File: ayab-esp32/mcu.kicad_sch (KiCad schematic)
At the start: 29 parts, among them J201 SPARE1, J202 SPARE0, Q201 AO3400A, SW201 USER, SW202 RESET, SW203 BOOTSEL, U201 ESP32-S3-MINI-1

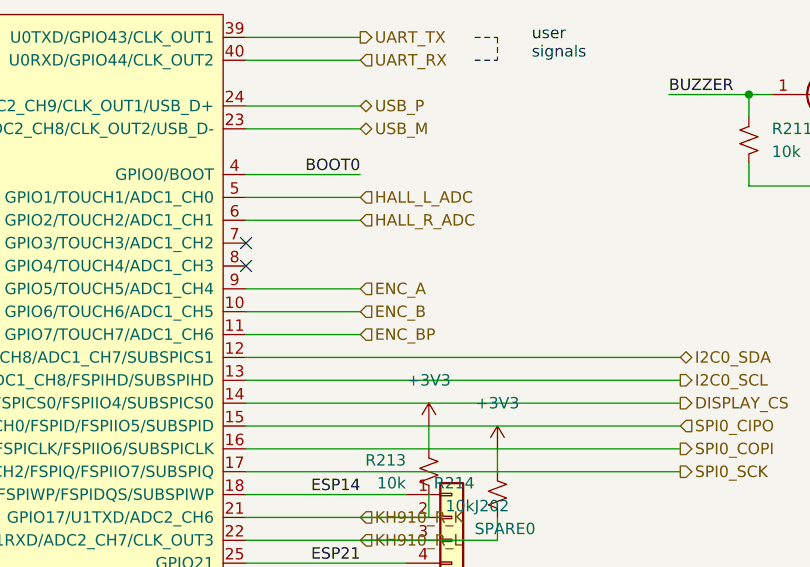
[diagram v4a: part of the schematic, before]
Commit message: Add machine power sensing on GPIO4
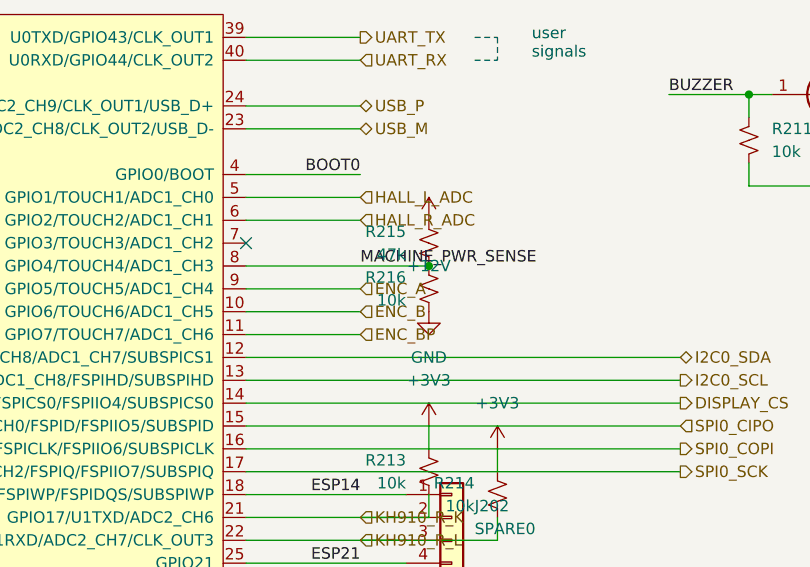
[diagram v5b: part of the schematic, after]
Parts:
- added R215: 47k, Resistor_SMD:R_0603_1608Metric, symbol ayab-lib:R_Small_US
- added R216: 10k, Resistor_SMD:R_0603_1608Metric, symbol ayab-lib:R_Small_US
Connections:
- net GND: now also R216.2
- net MACHINE_PWR_SENSE: now reaches U201.8 (GPIO4/TOUCH4/ADC1_CH3)
- net MACHINE_PWR_SENSE: now also R215.2, R216.1
- new net +12V: R215.1
- no-connect marks 8 -> 7
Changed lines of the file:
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@@
   (junction (at 41.91 99.06) (diameter 0) (color 0 0 0 0)
   )
-  (no_connect (at 185.42 82.55))
   (no_connect (at 185.42 80.01))
   (no_connect (at 93.98 128.27))
@@
   (no_connect (at 259.08 44.45))
   (no_connect (at 93.98 115.57))
+  (wire (pts (xy 185.42 82.55) (xy 205.74 82.55))
+    (stroke (width 0) (type default))
+  )
+  (junction (at 205.74 82.55) (diameter 0) (color 0 0 0 0)
+  )
+  (label "MACHINE_PWR_SENSE" (at 198.12 82.55 0) (fields_autoplaced)
+    (effects (font (size 1.27 1.27)) (justify left bottom))
+  )
   (wire (pts (xy 87.63 45.72) (xy 87.63 57.15))
     (stroke (width 0) (type default))
@@
         )
       )
+    )
+  )
+(symbol (lib_id "ayab-lib:R_Small_US") (at 205.74 80.01 0) (unit 1)
+    (in_bom yes) (on_board yes) (dnp no)
+    (property "Reference" "R215" (at 203.2 78.74 0)
+      (effects (font (size 1.27 1.27)) (justify right))
+    )
+    (property "Value" "47k" (at 203.2 81.28 0)
+      (effects (font (size 1.27 1.27)) (justify right))
+    )
+    (property "Footprint" "Resistor_SMD:R_0603_1608Metric" (at 205.74 80.01 0)
+      (effects (font (size 1.27 1.27)) hide)
+    )
+    (property "Datasheet" "~" (at 205.74 80.01 0)
+      (effects (font (size 1.27 1.27)) hide)
+    )
+    (property "LCSC ID" "C25819" (at 205.74 80.01 0)
+      (effects (font (size 1.27 1.27)) hide)
+    )
+    (property "Voltage rating" "" (at 205.74 80.01 0)
+      (effects (font (size 1.27 1.27)) hide)
+    )
+    (property "Package" "0603" (at 205.74 80.01 0)
+      (effects (font (size 1.27 1.27)) hide)
+    )
+    (property "OEM PN" "0603WAF4702T5E" (at 205.74 80.01 0)
+      (effects (font (size 1.27 1.27)) hide)
+    )
+    (property "OEM" "UNI-ROYAL(Uniroyal Elec)" (at 205.74 80.01 0)
+      (effects (font (size 1.27 1.27)) hide)
+    )
+    (pin "1")
+    (pin "2")
+    (instances
+      (project "ayab-esp32"
+        (path "/ad16b75f-afc8-4717-a7c6-8dd7b69a18e2/a7e0db0f-e473-44d4-a2fe-681f732aacb2"
+          (reference "R215") (unit 1)
+        )
+      )
+    )
+  )
+(symbol (lib_id "ayab-lib:R_Small_US") (at 205.74 85.09 0) (unit 1)
+    (in_bom yes) (on_board yes) (dnp no)
+    (property "Reference" "R216" (at 203.2 83.82 0)
+      (effects (font (size 1.27 1.27)) (justify right))
+    )
+    (property "Value" "10k" (at 203.2 86.36 0)
+      (effects (font (size 1.27 1.27)) (justify right))
+    )
+    (property "Footprint" "Resistor_SMD:R_0603_1608Metric" (at 205.74 85.09 0)
+      (effects (font (size 1.27 1.27)) hide)
+    )
+    (property "Datasheet" "~" (at 205.74 85.09 0)
+      (effects (font (size 1.27 1.27)) hide)
+    )
+    (property "LCSC ID" "C25804" (at 205.74 85.09 0)
+      (effects (font (size 1.27 1.27)) hide)
+    )
+    (property "Voltage rating" "" (at 205.74 85.09 0)
+      (effects (font (size 1.27 1.27)) hide)
+    )
+    (property "Package" "0603" (at 205.74 85.09 0)
+      (effects (font (size 1.27 1.27)) hide)
+    )
+    (property "OEM PN" "0603WAF1002T5E" (at 205.74 85.09 0)
+      (effects (font (size 1.27 1.27)) hide)
+    )
+    (property "OEM" "UNI-ROYAL(Uniroyal Elec)" (at 205.74 85.09 0)
+      (effects (font (size 1.27 1.27)) hide)
+    )
+    (pin "1")
+    (pin "2")
+    (instances
+      (project "ayab-esp32"
+        (path "/ad16b75f-afc8-4717-a7c6-8dd7b69a18e2/a7e0db0f-e473-44d4-a2fe-681f732aacb2"
+          (reference "R216") (unit 1)
+        )
+      )
+    )
+  )
+(symbol (lib_id "power:+12V") (at 205.74 77.47 0) (unit 1)
+    (in_bom yes) (on_board yes) (dnp no) (fields_autoplaced)
+    (property "Reference" "#PWR222" (at 205.74 83.82 0)
+      (effects (font (size 1.27 1.27)) hide)
+    )
+    (property "Value" "+12V" (at 205.74 82.55 0)
+      (effects (font (size 1.27 1.27)))
+    )
+    (property "Footprint" "" (at 205.74 77.47 0)
+      (effects (font (size 1.27 1.27)) hide)
+    )
+    (property "Datasheet" "" (at 205.74 77.47 0)
+      (effects (font (size 1.27 1.27)) hide)
+    )
+    (pin "1")
+    (instances
+      (project "ayab-esp32"
+        (path "/ad16b75f-afc8-4717-a7c6-8dd7b69a18e2/a7e0db0f-e473-44d4-a2fe-681f732aacb2"
+          (reference "#PWR222") (unit 1)
+        )
+      )
+    )
+  )
+(symbol (lib_id "power:GND") (at 205.74 87.63 0) (unit 1)
+    (in_bom yes) (on_board yes) (dnp no) (fields_autoplaced)
+    (property "Reference" "#PWR223" (at 205.74 93.98 0)
+      (effects (font (size 1.27 1.27)) hide)
+    )
+    (property "Value" "GND" (at 205.74 92.71 0)
+      (effects (font (size 1.27 1.27)))
+    )
+    (property "Footprint" "" (at 205.74 87.63 0)
+      (effects (font (size 1.27 1.27)) hide)
+    )
+    (property "Datasheet" "" (at 205.74 87.63 0)
+      (effects (font (size 1.27 1.27)) hide)
+    )
+    (pin "1")
+    (instances
+      (project "ayab-esp32"
+        (path "/ad16b75f-afc8-4717-a7c6-8dd7b69a18e2/a7e0db0f-e473-44d4-a2fe-681f732aacb2"
+          (reference "#PWR223") (unit 1)
+        )
+      )

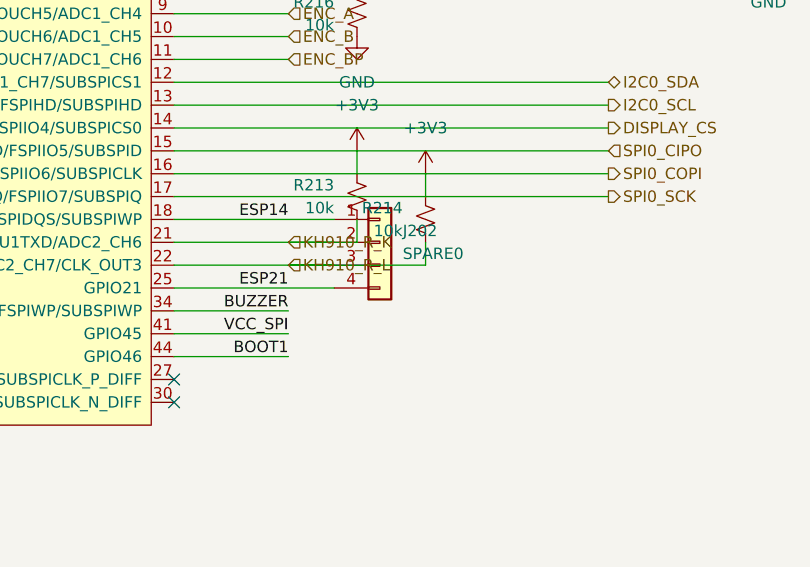
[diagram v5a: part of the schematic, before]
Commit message: Add hardware-default-OFF solenoid power gate
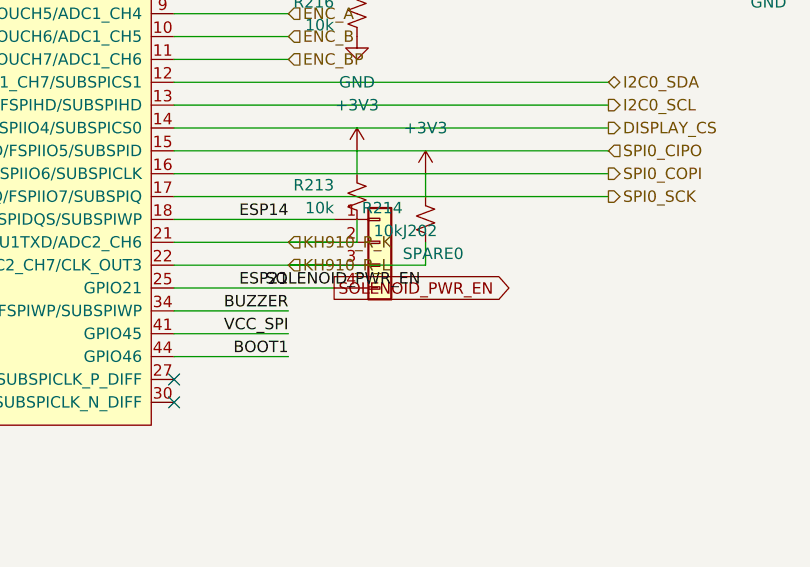
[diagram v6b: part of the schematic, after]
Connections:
- net ESP21 renamed SOLENOID_PWR_EN
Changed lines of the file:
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@@
   (no_connect (at 259.08 44.45))
   (no_connect (at 93.98 115.57))
+  (label "SOLENOID_PWR_EN" (at 195.58 115.57 0) (fields_autoplaced)
+    (effects (font (size 1.27 1.27)) (justify left bottom))
+  )
+  (global_label "SOLENOID_PWR_EN" (shape output) (at 203.2 115.57 0) (fields_autoplaced)
+    (effects (font (size 1.27 1.27)) (justify left))
+  )
   (wire (pts (xy 185.42 82.55) (xy 205.74 82.55))
     (stroke (width 0) (type default))

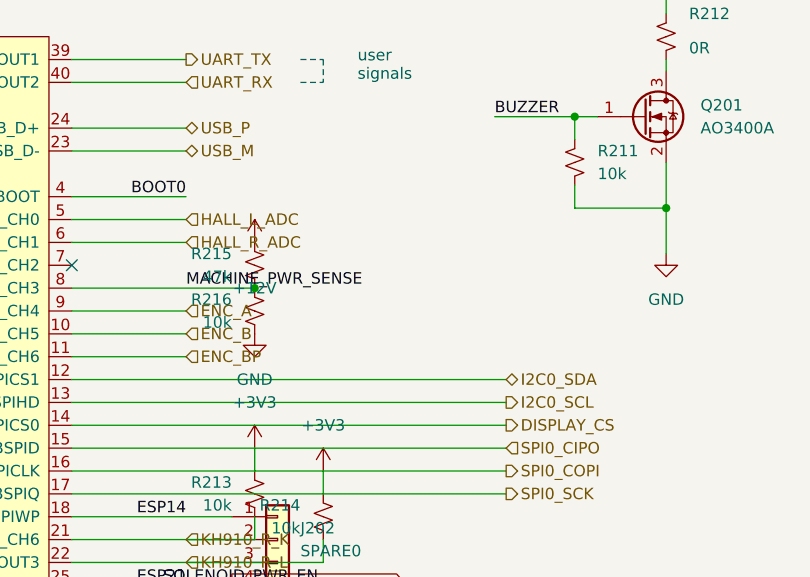
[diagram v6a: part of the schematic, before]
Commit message: Integrate protected machine-power sensing
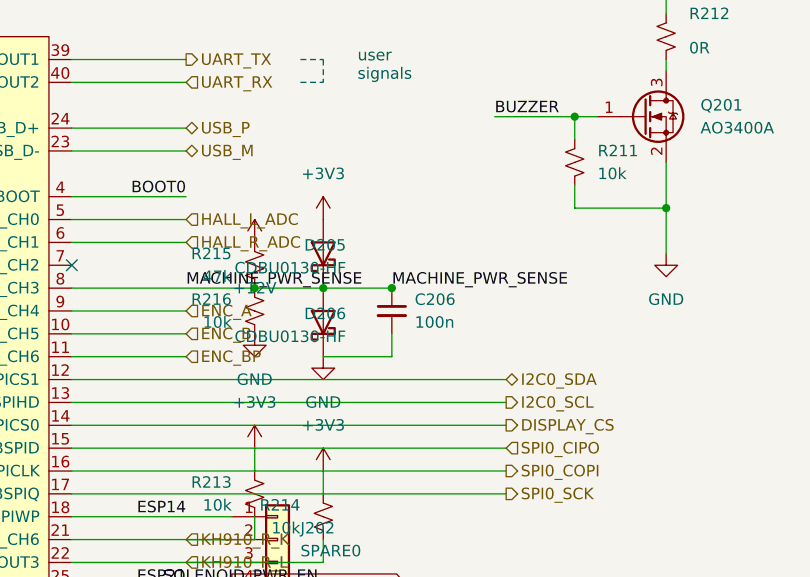
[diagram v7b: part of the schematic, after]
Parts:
- added C206: 100n, Capacitor_SMD:C_0603_1608Metric, symbol ayab-lib:C_Small
- added D205, D206: CDBU0130-HF, Diode_SMD:D_0603_1608Metric, symbol ayab-lib:D_Schottky
- C201, C202, C203, C204: LCSC ID C57112 -> C14663; OEM FH (Guangdong Fenghua Advanced Tech) -> Samsung Electro-Mechanics; OEM PN 0603B103K500NT -> CL10B104KB8NNNC; Voltage rating 24V X7R -> 50V X7R
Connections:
- net +3V3: now also D205.2 (A)
- net GND: now also C206.2, D206.1 (K)
- net MACHINE_PWR_SENSE: now also C206.1, D205.1 (K), D206.2 (A)
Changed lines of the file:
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@@
     (effects (font (size 1.27 1.27)) (justify left))
   )
+  (label "MACHINE_PWR_SENSE" (at 220.98 82.55 0) (fields_autoplaced)
+    (effects (font (size 1.27 1.27)) (justify left bottom))
+  )
+  (wire (pts (xy 205.74 82.55) (xy 220.98 82.55))
+    (stroke (width 0) (type default))
+  )
+  (wire (pts (xy 220.98 87.63) (xy 220.98 90.17))
+    (stroke (width 0) (type default))
+  )
+  (wire (pts (xy 213.36 90.17) (xy 220.98 90.17))
+    (stroke (width 0) (type default))
+  )
+  (junction (at 213.36 82.55) (diameter 0) (color 0 0 0 0)
+  )
+  (junction (at 220.98 82.55) (diameter 0) (color 0 0 0 0)
+  )
   (wire (pts (xy 185.42 82.55) (xy 205.74 82.55))
     (stroke (width 0) (type default))
@@
       (effects (font (size 1.27 1.27)) hide)
     )
-    (property "LCSC ID" "C57112" (at 154.94 41.91 0)
+    (property "LCSC ID" "C14663" (at 154.94 41.91 0)
       (effects (font (size 1.27 1.27)) hide)
     )
-    (property "Voltage rating" "24V X7R" (at 154.94 41.91 0)
+    (property "Voltage rating" "50V X7R" (at 154.94 41.91 0)
       (effects (font (size 1.27 1.27)) hide)
     )
@@
       (effects (font (size 1.27 1.27)) hide)
     )
-    (property "OEM PN" "0603B103K500NT" (at 154.94 41.91 0)
+    (property "OEM PN" "CL10B104KB8NNNC" (at 154.94 41.91 0)
       (effects (font (size 1.27 1.27)) hide)
     )
-    (property "OEM" "FH (Guangdong Fenghua Advanced Tech)" (at 154.94 41.91 0)
+    (property "OEM" "Samsung Electro-Mechanics" (at 154.94 41.91 0)
       (effects (font (size 1.27 1.27)) hide)
     )
@@
       (effects (font (size 1.27 1.27)) hide)
     )
-    (property "LCSC ID" "C57112" (at 78.74 50.8 0)
+    (property "LCSC ID" "C14663" (at 78.74 50.8 0)
       (effects (font (size 1.27 1.27)) hide)
     )
-    (property "Voltage rating" "24V X7R" (at 78.74 50.8 0)
+    (property "Voltage rating" "50V X7R" (at 78.74 50.8 0)
       (effects (font (size 1.27 1.27)) hide)
     )
@@
       (effects (font (size 1.27 1.27)) hide)
     )
-    (property "OEM PN" "0603B103K500NT" (at 78.74 50.8 0)
+    (property "OEM PN" "CL10B104KB8NNNC" (at 78.74 50.8 0)
       (effects (font (size 1.27 1.27)) hide)
     )
-    (property "OEM" "FH (Guangdong Fenghua Advanced Tech)" (at 78.74 50.8 0)
+    (property "OEM" "Samsung Electro-Mechanics" (at 78.74 50.8 0)
       (effects (font (size 1.27 1.27)) hide)
     )
@@
       (effects (font (size 1.27 1.27)) hide)
     )
-    (property "LCSC ID" "C57112" (at 45.72 129.54 0)
+    (property "LCSC ID" "C14663" (at 45.72 129.54 0)
       (effects (font (size 1.27 1.27)) hide)
     )
-    (property "Voltage rating" "24V X7R" (at 45.72 129.54 0)
+    (property "Voltage rating" "50V X7R" (at 45.72 129.54 0)
       (effects (font (size 1.27 1.27)) hide)
     )
@@
       (effects (font (size 1.27 1.27)) hide)
     )
-    (property "OEM PN" "0603B103K500NT" (at 45.72 129.54 0)
+    (property "OEM PN" "CL10B104KB8NNNC" (at 45.72 129.54 0)
       (effects (font (size 1.27 1.27)) hide)
     )
-    (property "OEM" "FH (Guangdong Fenghua Advanced Tech)" (at 45.72 129.54 0)
+    (property "OEM" "Samsung Electro-Mechanics" (at 45.72 129.54 0)
       (effects (font (size 1.27 1.27)) hide)
     )
@@
       (effects (font (size 1.27 1.27)) hide)
     )
-    (property "LCSC ID" "C57112" (at 144.78 41.91 0)
+    (property "LCSC ID" "C14663" (at 144.78 41.91 0)
       (effects (font (size 1.27 1.27)) hide)
     )
-    (property "Voltage rating" "24V X7R" (at 144.78 41.91 0)
+    (property "Voltage rating" "50V X7R" (at 144.78 41.91 0)
       (effects (font (size 1.27 1.27)) hide)
     )
@@
       (effects (font (size 1.27 1.27)) hide)
     )
-    (property "OEM PN" "0603B103K500NT" (at 144.78 41.91 0)
+    (property "OEM PN" "CL10B104KB8NNNC" (at 144.78 41.91 0)
       (effects (font (size 1.27 1.27)) hide)
     )
-    (property "OEM" "FH (Guangdong Fenghua Advanced Tech)" (at 144.78 41.91 0)
+    (property "OEM" "Samsung Electro-Mechanics" (at 144.78 41.91 0)
       (effects (font (size 1.27 1.27)) hide)
     )
@@
         )
       )
+    )
+  )
+(symbol (lib_id "ayab-lib:D_Schottky") (at 213.36 78.74 90) (unit 1)
+    (in_bom yes) (on_board yes) (dnp no) (fields_autoplaced)
+    (property "Reference" "D205" (at 215.9 77.7875 90)
+      (effects (font (size 1.27 1.27)) (justify left))
+    )
+    (property "Value" "CDBU0130-HF" (at 215.9 80.3275 90)
+      (effects (font (size 1.27 1.27)) (justify left))
+    )
+    (property "Footprint" "Diode_SMD:D_0603_1608Metric" (at 213.36 78.74 0)
+      (effects (font (size 1.27 1.27)) hide)
+    )
+    (property "Datasheet" "https://datasheet.lcsc.com/lcsc/2205091530_Comchip-Technology-CDBU0130-HF_C2886021.pdf" (at 213.36 78.74 0)
+      (effects (font (size 1.27 1.27)) hide)
+    )
+    (property "Package" "0603/SOD-523F" (at 213.36 78.74 0)
+      (effects (font (size 1.27 1.27)) hide)
+    )
+    (property "LCSC ID" "C2886021" (at 213.36 78.74 0)
+      (effects (font (size 1.27 1.27)) hide)
+    )
+    (property "OEM PN" "CDBU0130-HF" (at 213.36 78.74 0)
+      (effects (font (size 1.27 1.27)) hide)
+    )
+    (property "OEM" "Comchip Technology" (at 213.36 78.74 0)
+      (effects (font (size 1.27 1.27)) hide)
+    )
+    (pin "1")
+    (pin "2")
+    (instances
+      (project "ayab-esp32"
+        (path "/ad16b75f-afc8-4717-a7c6-8dd7b69a18e2/aaa14c5f-6969-439e-bdef-bb5fc66f917d"
+          (reference "D205") (unit 1)
+        )
+      )
+    )
+  )
+(symbol (lib_id "ayab-lib:D_Schottky") (at 213.36 86.36 90) (unit 1)
+    (in_bom yes) (on_board yes) (dnp no) (fields_autoplaced)
+    (property "Reference" "D206" (at 215.9 85.4075 90)
+      (effects (font (size 1.27 1.27)) (justify left))
+    )
+    (property "Value" "CDBU0130-HF" (at 215.9 87.9475 90)
+      (effects (font (size 1.27 1.27)) (justify left))
+    )
+    (property "Footprint" "Diode_SMD:D_0603_1608Metric" (at 213.36 86.36 0)
+      (effects (font (size 1.27 1.27)) hide)
+    )
+    (property "Datasheet" "https://datasheet.lcsc.com/lcsc/2205091530_Comchip-Technology-CDBU0130-HF_C2886021.pdf" (at 213.36 86.36 0)
+      (effects (font (size 1.27 1.27)) hide)
+    )
+    (property "Package" "0603/SOD-523F" (at 213.36 86.36 0)
+      (effects (font (size 1.27 1.27)) hide)
+    )
+    (property "LCSC ID" "C2886021" (at 213.36 86.36 0)
+      (effects (font (size 1.27 1.27)) hide)
+    )
+    (property "OEM PN" "CDBU0130-HF" (at 213.36 86.36 0)
+      (effects (font (size 1.27 1.27)) hide)
+    )
+    (property "OEM" "Comchip Technology" (at 213.36 86.36 0)
+      (effects (font (size 1.27 1.27)) hide)
+    )
+    (pin "1")
+    (pin "2")
+    (instances
+      (project "ayab-esp32"
+        (path "/ad16b75f-afc8-4717-a7c6-8dd7b69a18e2/175ec455-5c18-4495-952f-cdd672f0311a"
+          (reference "D206") (unit 1)
+        )
+      )
+    )
+  )
+(symbol (lib_id "ayab-lib:C_Small") (at 220.98 85.09 0) (unit 1)
+    (in_bom yes) (on_board yes) (dnp no)
+    (property "Reference" "C206" (at 223.52 83.8263 0)
+      (effects (font (size 1.27 1.27)) (justify left))
+    )
+    (property "Value" "100n" (at 223.52 86.36 0)
+      (effects (font (size 1.27 1.27)) (justify left))
+    )
+    (property "Footprint" "Capacitor_SMD:C_0603_1608Metric" (at 220.98 85.09 0)
+      (effects (font (size 1.27 1.27)) hide)
+    )
+    (property "Datasheet" "~" (at 220.98 85.09 0)
+      (effects (font (size 1.27 1.27)) hide)
+    )
+    (property "LCSC ID" "C14663" (at 220.98 85.09 0)
+      (effects (font (size 1.27 1.27)) hide)
+    )
+    (property "Voltage rating" "50V X7R" (at 220.98 85.09 0)
+      (effects (font (size 1.27 1.27)) hide)
+    )
+    (property "Package" "0603" (at 220.98 85.09 0)
+      (effects (font (size 1.27 1.27)) hide)
+    )
+    (property "OEM PN" "CL10B104KB8NNNC" (at 220.98 85.09 0)
+      (effects (font (size 1.27 1.27)) hide)
+    )
+    (property "OEM" "Samsung Electro-Mechanics" (at 220.98 85.09 0)
+      (effects (font (size 1.27 1.27)) hide)
+    )
+    (pin "1")
+    (pin "2")
+    (instances
+      (project "ayab-esp32"
+        (path "/ad16b75f-afc8-4717-a7c6-8dd7b69a18e2/86d7191f-1078-449e-8193-ca35bc117e8d"
+          (reference "C206") (unit 1)
+        )
+      )
+    )
+  )
+(symbol (lib_id "power:+3V3") (at 213.36 74.93 0) (unit 1)
+    (in_bom yes) (on_board yes) (dnp no) (fields_autoplaced)
+    (property "Reference" "#PWR224" (at 213.36 78.74 0)
+      (effects (font (size 1.27 1.27)) hide)
+    )
+    (property "Value" "+3V3" (at 213.36 69.85 0)
+      (effects (font (size 1.27 1.27)))
+    )
+    (property "Footprint" "" (at 213.36 74.93 0)
+      (effects (font (size 1.27 1.27)) hide)
+    )
+    (property "Datasheet" "" (at 213.36 74.93 0)
+      (effects (font (size 1.27 1.27)) hide)
+    )
+    (pin "1")
+    (instances
+      (project "ayab-esp32"
+        (path "/ad16b75f-afc8-4717-a7c6-8dd7b69a18e2/d8ac7f65-44d2-4f41-8d2d-d53a9e10225f"
+          (reference "#PWR224") (unit 1)
+        )
+      )
+    )
+  )
+(symbol (lib_id "power:GND") (at 213.36 90.17 0) (unit 1)
+    (in_bom yes) (on_board yes) (dnp no) (fields_autoplaced)
+    (property "Reference" "#PWR225" (at 213.36 96.52 0)
+      (effects (font (size 1.27 1.27)) hide)
+    )
+    (property "Value" "GND" (at 213.36 95.25 0)
+      (effects (font (size 1.27 1.27)))
+    )
+    (property "Footprint" "" (at 213.36 90.17 0)
+      (effects (font (size 1.27 1.27)) hide)
+    )
+    (property "Datasheet" "" (at 213.36 90.17 0)
+      (effects (font (size 1.27 1.27)) hide)
+    )
+    (pin "1")
+    (instances
+      (project "ayab-esp32"
+        (path "/ad16b75f-afc8-4717-a7c6-8dd7b69a18e2/c17f12ba-01d6-4999-8932-e3a7d075613b"
+          (reference "#PWR225") (unit 1)
+        )
+      )
